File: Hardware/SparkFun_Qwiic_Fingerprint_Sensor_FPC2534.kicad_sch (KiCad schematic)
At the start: 41 parts, among them J1 Qwiic_RA, J2 Qwiic_RA, J4 USB_C_Receptacle, J5 Conn_01x06, J7 Conn_01x06, U1 FPC2354, U2 RT9080-3.3

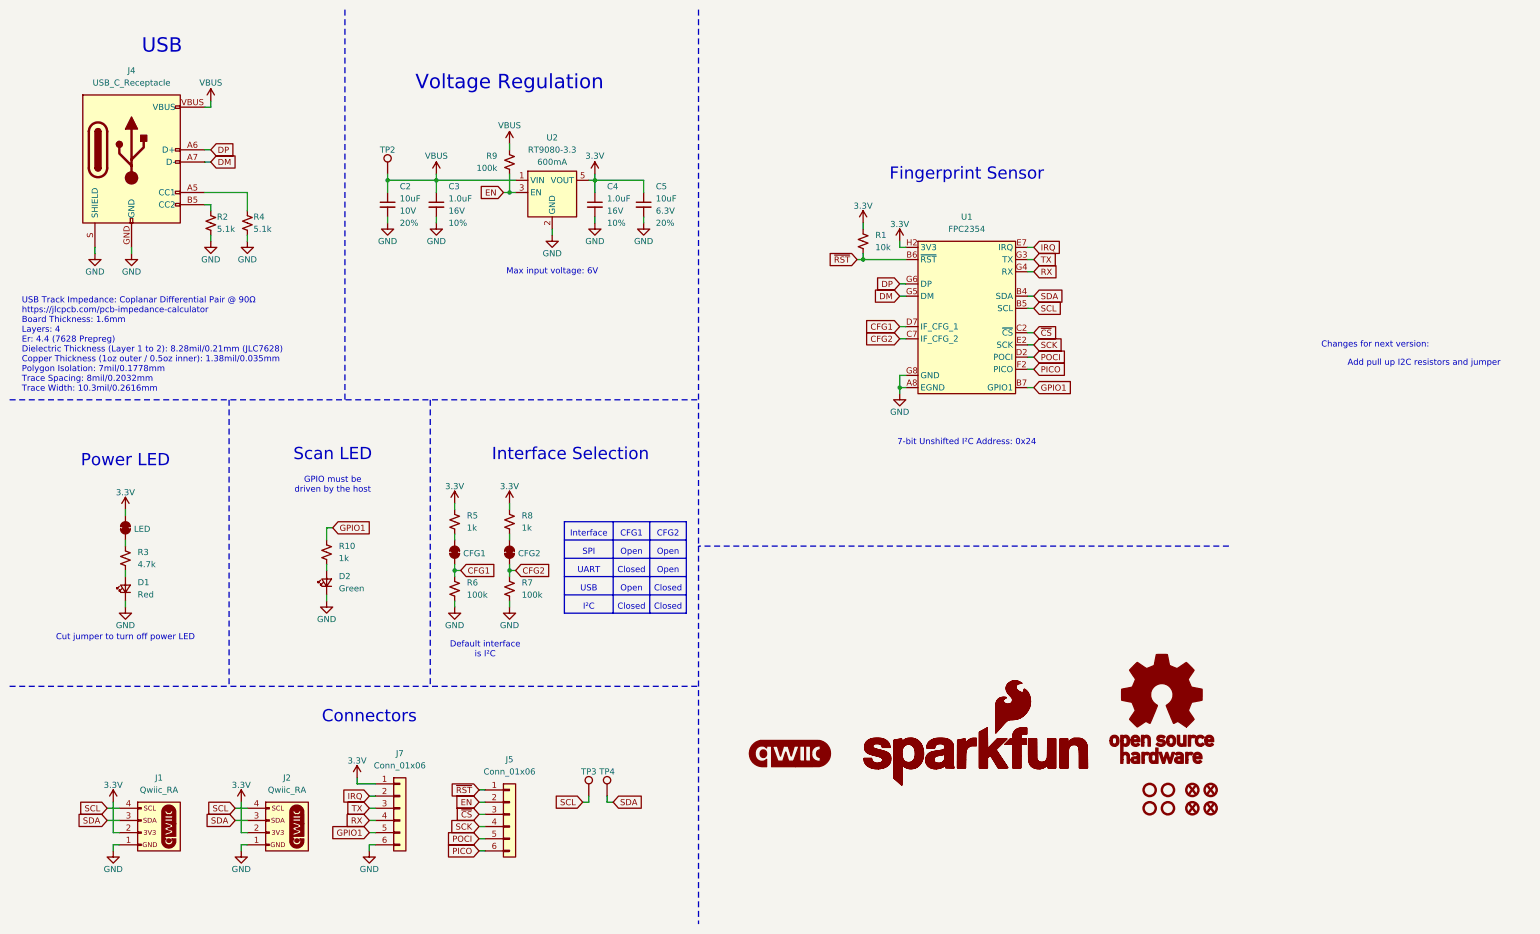
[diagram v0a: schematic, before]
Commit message: Add I2C pull ups and jumper. Adjust silk.
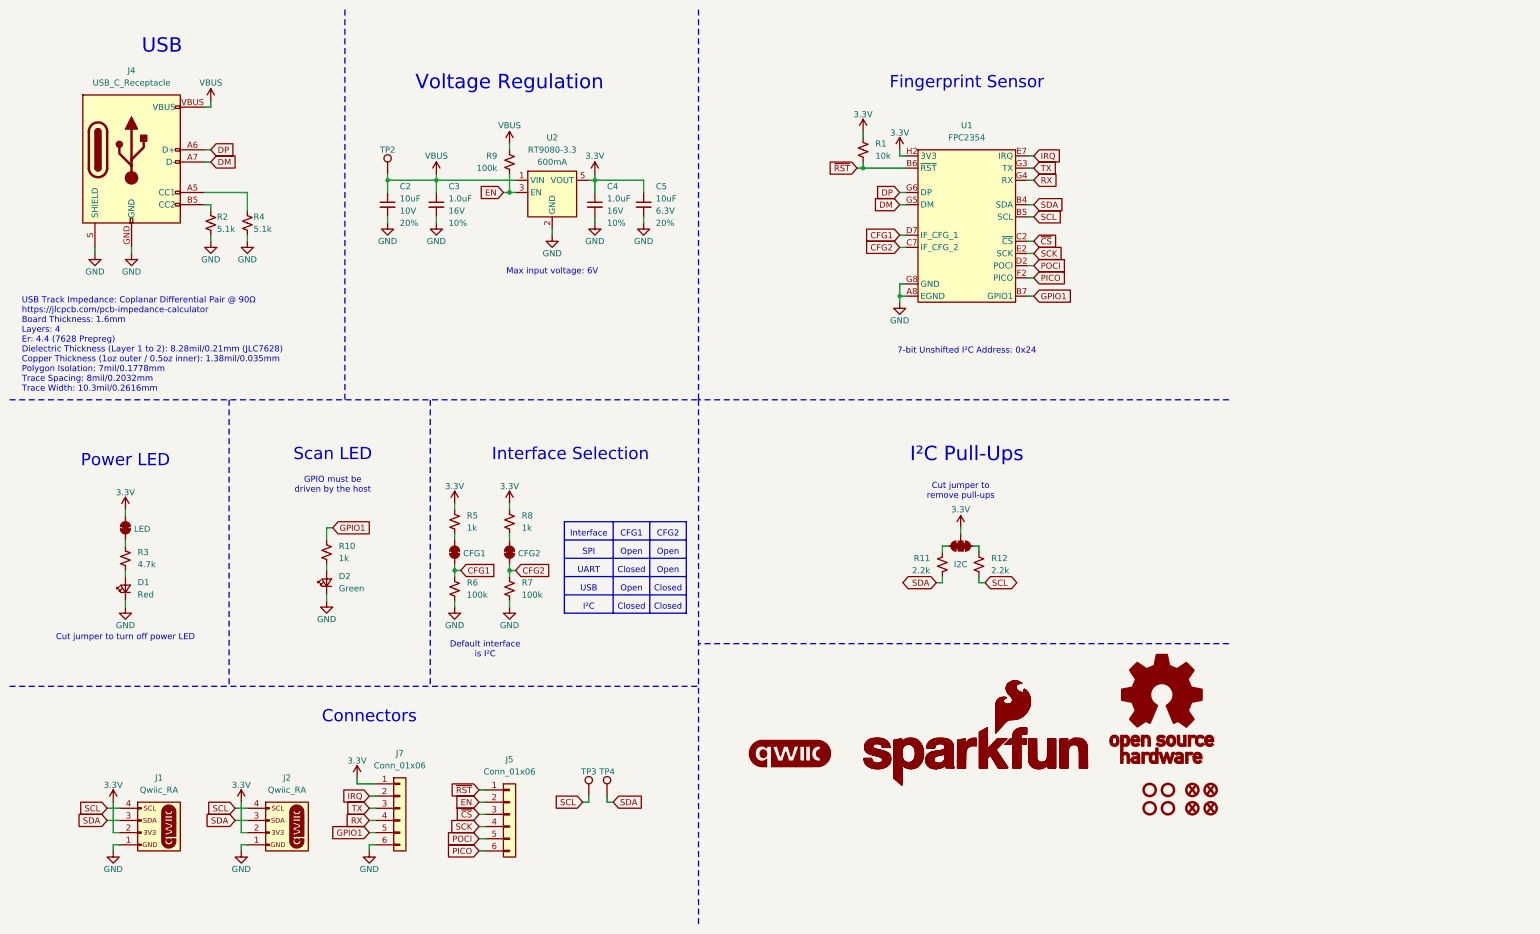
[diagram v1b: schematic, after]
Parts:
- added JP4: I2C, SparkFun-Jumper:Jumper_3_NC-2_Trace, symbol SparkFun-Jumper:SolderJumper_3_Bridged123
- added R11, R12: 2.2k, SparkFun-Resistor:R_0603_1608Metric, symbol SparkFun-Resistor:2.2k_0603
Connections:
- net 3.3V: now also JP4.2 (B)
- net SCL: now also R12.1
- net SDA: now also R11.1
- new net: JP4.1 (A), R12.2
- new net: JP4.3 (C), R11.2
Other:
- note added: "Cut jumper to remove pull-ups"
- note added: "I²C Pull-Ups"
- note removed: "Add pull up I2C resistors and jumper"
- note removed: "Changes for next version:"
- moved on the sheet: R1, U1

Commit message: Post design review.
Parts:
- removed ST1, ST2, ST3, ST4: Standoff, SparkFun-Hardware:Standoff, symbol SparkFun-Hardware:Standoff
- removed TP3, TP4: TestPoint_0.75mm, SparkFun-Connector:TestPoint-0.75mm, symbol SparkFun-Connector:TestPoint_0.75mm
- added J3, J6: Conn_01x01, SparkFun-Connector:1x01, symbol SparkFun-Connector:Conn_01x01
- added JP5: BZL, SparkFun-Jumper:Jumper_2_NC_Trace, symbol SparkFun-Jumper:SolderJumper_2_Bridged
- added ST5, ST6, ST7, ST8: Standoff, SparkFun-Hardware:Standoff_Connected, symbol SparkFun-Hardware:Standoff_Connected
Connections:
- net EGND: now also JP5.1 (A), ST5.1, ST6.1, ST7.1, ST8.1; no longer C2.2, C3.2, C4.2, C5.2, D1.1 (K), D2.1 (K), J1.1 (Pin_1), J2.1 (Pin_1), J4.GND, J4.S (SHIELD), J7.6 (Pin_6), R2.1, R4.1, R6.1, R7.1, U1.B1 (GND), U1.B8 (GND), U1.G1 (GND), U1.G8 (GND), U2.2 (GND)
- net SCL: now also J3.1 (Pin_1)
- net SDA: now also J6.1 (Pin_1)
- new net GND: C2.2, C3.2, C4.2, C5.2, D1.1 (K), D2.1 (K), J1.1 (Pin_1), J2.1 (Pin_1), J4.GND, J4.S (SHIELD), J7.6 (Pin_6), JP5.2 (B), R2.1, R4.1, R6.1, R7.1, U1.B1 (GND), U1.B8 (GND), U1.G1 (GND), U1.G8 (GND), U2.2 (GND)
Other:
- note added: "Cut BZL to isolate bezel connections from ground"
- note added: "Driven via software command"
- note removed: "GPIO must be driven by the host"
- note removed: "Max input voltage: 6V"
